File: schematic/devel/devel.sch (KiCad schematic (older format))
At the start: 108 parts

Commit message: converted schematic to flat hierarchical
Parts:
- removed C? (x2): 330n, symbol Device:C_Small
- removed C? (x2): 10u, symbol Device:CP_Small
- removed C? (x3): 1u, symbol Device:CP_Small
- removed C?: 22u, symbol Device:C_Small
- removed C?: 2.2u, symbol Device:CP_Small
- removed C? (x11): 100n, symbol Device:C_Small
- removed C?: 10n, symbol Device:C_Small
- removed C? (x4): 4p, symbol Device:C_Small
- removed D? (x4): 1N4001, Diode_THT:D_DO-41_SOD81_P10.16mm_Horizontal, symbol Diode:1N4001
- removed D?: S599x, symbol common:S599x
- removed D? (x2): 1N4148, Diode_THT:D_DO-35_SOD27_P7.62mm_Horizontal, symbol Diode:1N4148
- removed J?: CONN_PWR, symbol Connector:Conn_01x03_Male
- removed J?: X1, symbol Connector:Conn_Coaxial
- removed J?: X2, symbol Connector:Conn_Coaxial
- removed J?: Y1, symbol Connector:Conn_Coaxial
- removed J?: Y2, symbol Connector:Conn_Coaxial
- removed J?: DIFFX, symbol Connector:Conn_Coaxial
- removed J?: DIFFY, symbol Connector:Conn_Coaxial
- removed J?: SUM, symbol Connector:Conn_Coaxial
- removed J?: POSX, symbol Connector:Conn_Coaxial
- removed J?: POSY, symbol Connector:Conn_Coaxial
- removed R?: 100, symbol Device:R_Small
- removed R? (x4): 100k, symbol Device:R_Small
- removed R? (x18): 1k, symbol Device:R_Small
- removed R? (x9): 50, symbol Device:R_Small
- removed TP? (x6): TestPoint, symbol Connector:TestPoint
- removed U?: REF5010IDGK, Package_SO:MSOP-8_3x3mm_P0.65mm, symbol Reference_Voltage:REF5010IDGK
- removed U?: L7812, symbol Regulator_Linear:L7812
- removed U?: L7912, symbol Regulator_Linear:L7912
- removed U? (x23): OPA4197, symbol Device:Opamp_Quad_Generic
- removed U? (x2): AD538, symbol common:AD538
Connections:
- net labels removed: +10V, +12V, +15V, -12V, -15V, -X1, -X2, -Y1, -Y2, DIFFX, DIFFY, GND, POSX, POSY, SUM
- wire segments 398 -> 0
- no-connect marks 20 -> 0
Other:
- note removed: "BIAS VOLTAGE"
- note removed: "BUFFERED OUTPUT CONNECTORS"
- note removed: "DIVISION ARTHIMETIC"
- note removed: "LINEAR ARTHIMETIC"
- note removed: "POSITION-SENSITIVE DETECTOR AND TRANSIMPEDANCE AMPLIFIER"
- note removed: "POWER CONNECTOR"
- note removed: "SUPPLY VOLTAGE"

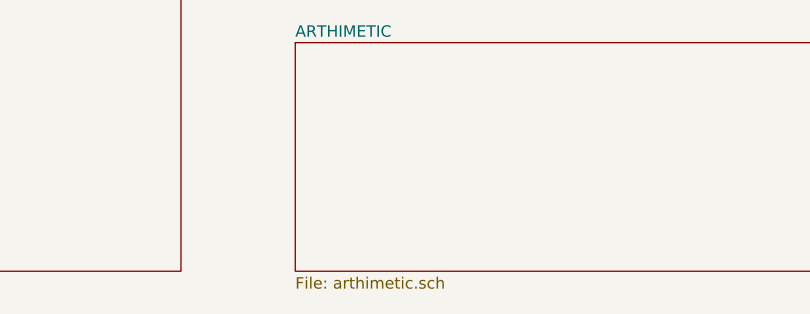
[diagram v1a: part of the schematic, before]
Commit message: fixed arithmetic typo, decoupling cap polarisation
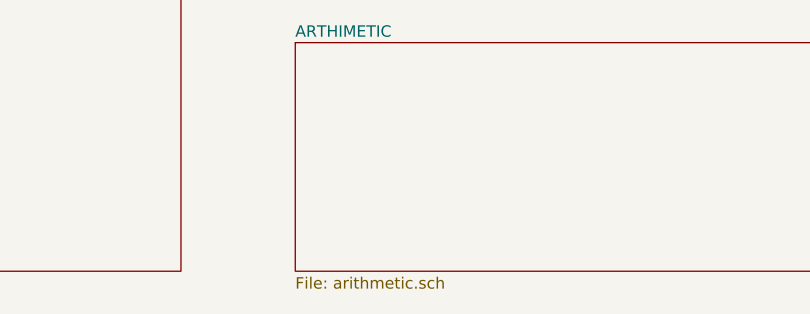
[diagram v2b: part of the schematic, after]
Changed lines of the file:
@@
 U 5D894F76
 F0 "ARTHIMETIC" 50
-F1 "arthimetic.sch" 50
+F1 "arithmetic.sch" 50
 $EndSheet
 $Sheet

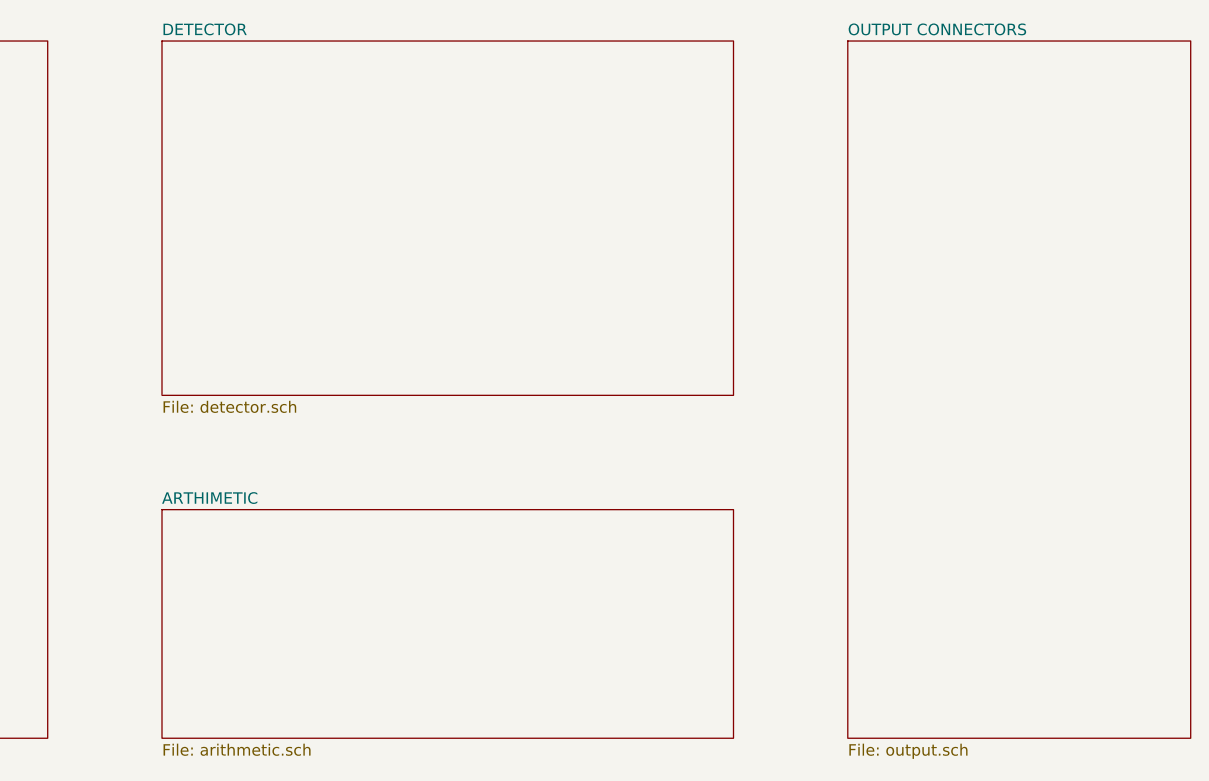
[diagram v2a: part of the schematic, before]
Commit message: removed arithmetic unit from development board, changed output connectors
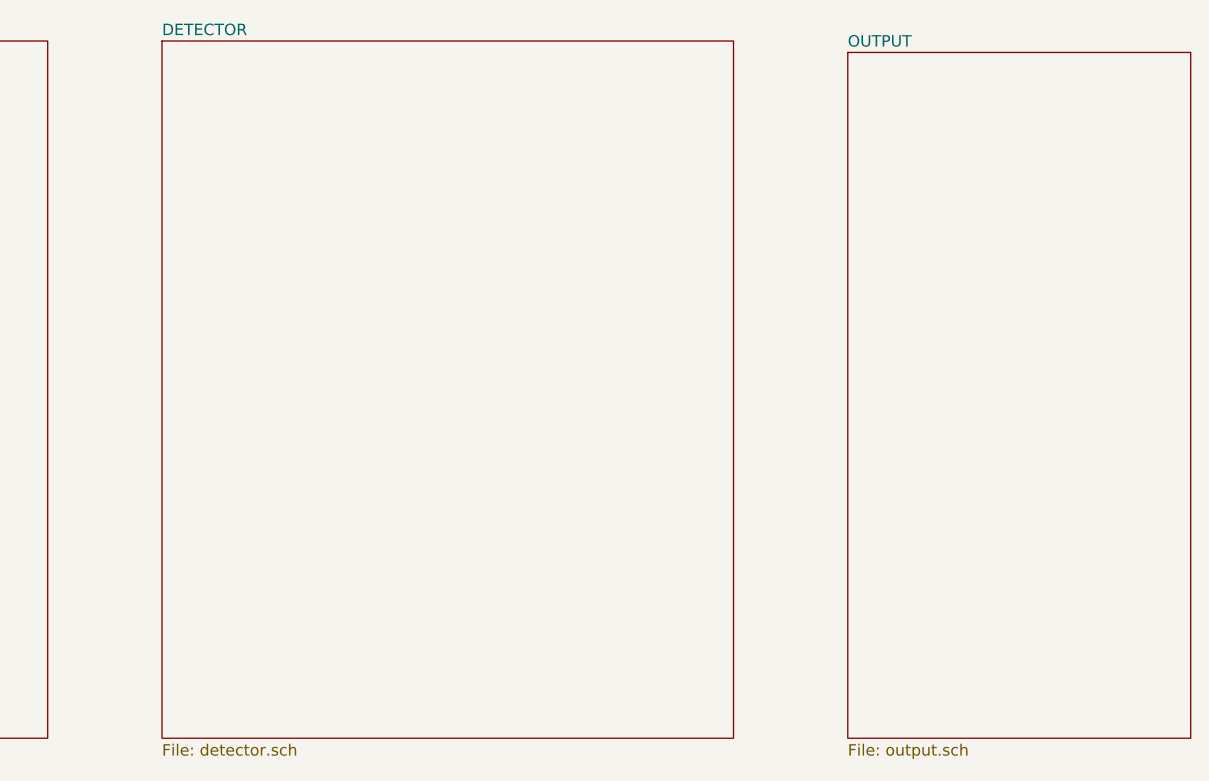
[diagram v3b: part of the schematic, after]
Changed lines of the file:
@@
 $Descr A4 11693 8268
 encoding utf-8
-Sheet 1 5
+Sheet 1 4
 Title "Position-sensitive Detector Development Board"
 Date "2019-03-21"
@@
 $EndSheet
 $Sheet
-S 4500 4500 2500 1000
-U 5D894F76
-F0 "ARTHIMETIC" 50
-F1 "arithmetic.sch" 50
-$EndSheet
-$Sheet
-S 7500 2450 1500 3050
-U 5D911A34
-F0 "OUTPUT CONNECTORS" 50
-F1 "output.sch" 50
-$EndSheet
-$Sheet
-S 4500 2450 2500 1550
+S 4500 2450 2500 3050
 U 5D929D0E
 F0 "DETECTOR" 50
 F1 "detector.sch" 50
 $EndSheet
+$Sheet
+S 7500 2500 1500 3000
+U 5C9BDA7E
+F0 "OUTPUT" 50
+F1 "output.sch" 50
+$EndSheet
 $EndSCHEMATC

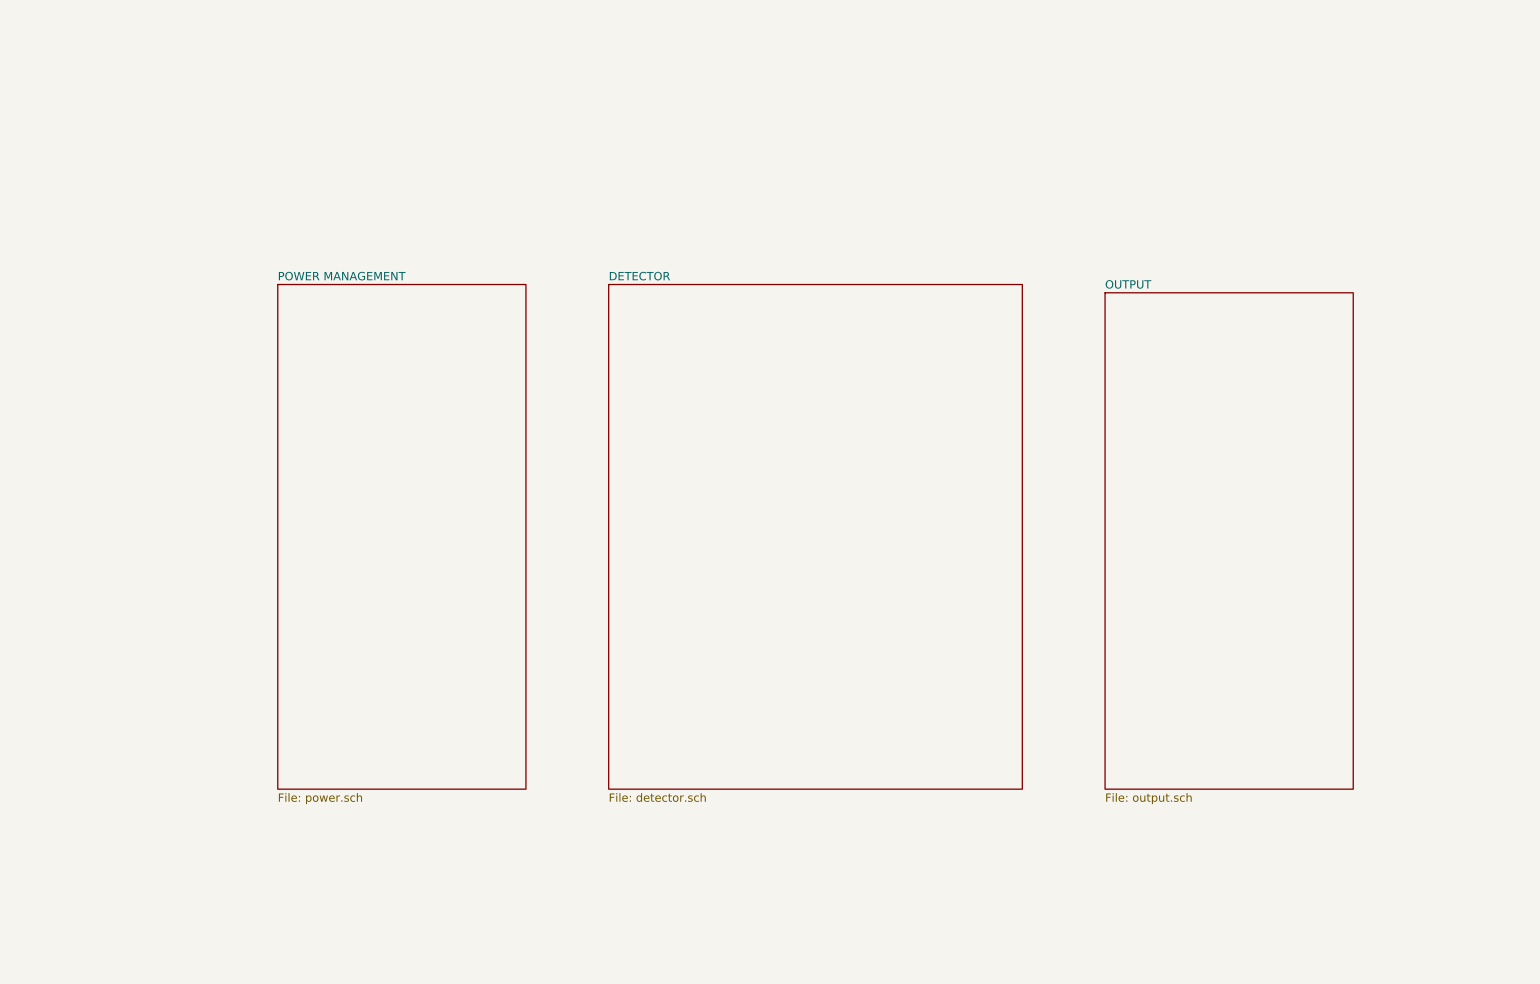
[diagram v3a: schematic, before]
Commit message: merged circuit sheets to single sheet, removed extra diodes, changed diode type
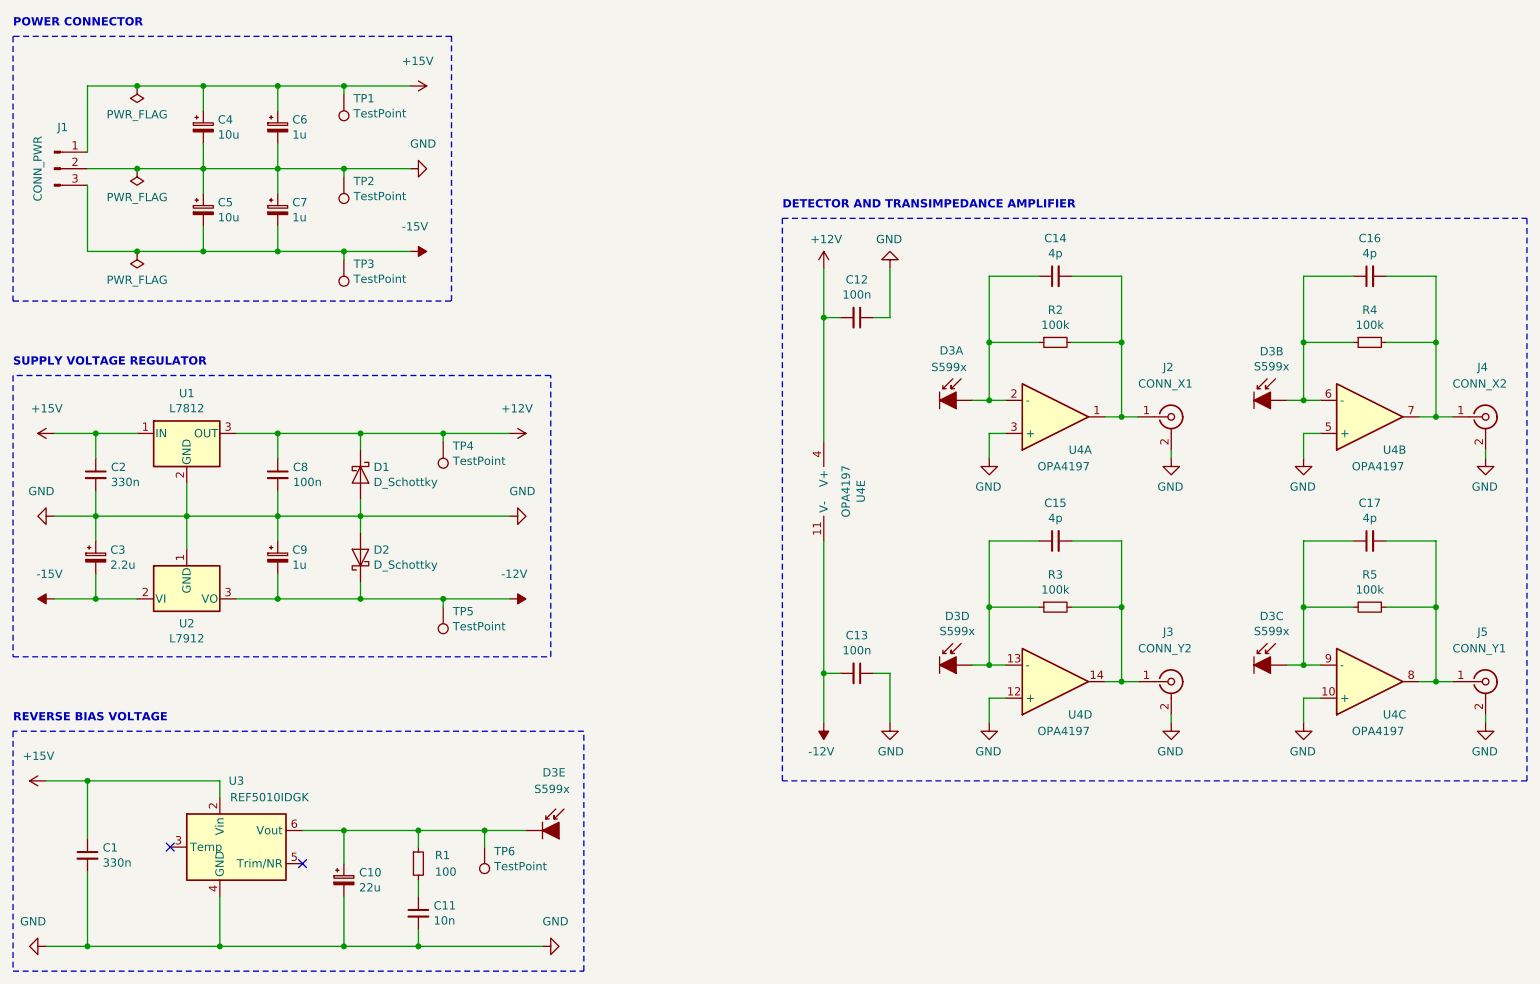
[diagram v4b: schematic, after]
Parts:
- added C1: 330n, Capacitor_SMD:C_0603_1608Metric, symbol Device:C_Small
- added C10: 22u, Capacitor_SMD:CP_Elec_5x5.4, symbol Device:CP_Small
- added C11: 10n, Capacitor_SMD:C_0402_1005Metric, symbol Device:C_Small
- added C12, C13, C8: 100n, Capacitor_SMD:C_0603_1608Metric, symbol Device:C_Small
- added C14, C15, C16, C17: 4p, Capacitor_SMD:C_0402_1005Metric, symbol Device:C_Small
- added C2: 330n, Capacitor_SMD:C_0805_2012Metric, symbol Device:C_Small
- added C3: 2.2u, Capacitor_SMD:CP_Elec_4x5.4, symbol Device:CP_Small
- added C4, C5: 10u, Capacitor_SMD:CP_Elec_4x5.4, symbol Device:CP_Small
- added C6, C7: 1u, Capacitor_SMD:CP_Elec_4x5.4, symbol Device:CP_Small
- added C9: 1u, Capacitor_SMD:CP_Elec_5x4.4, symbol Device:CP_Small
- added D1, D2: D_Schottky, Diode_SMD:D_SMA, symbol Device:D_Schottky
- added D3: S599x, Sensor_OpticalPosition:S5990, symbol Sensor_OpticalPosition:S599x
- added J1: CONN_PWR, Connector_PinHeader_1.00mm:PinHeader_1x03_P1.00mm_Vertical, symbol Connector:Conn_01x03_Male
- added J2: CONN_X1, Connector_Coaxial:SMA_Amphenol_901-144_Vertical, symbol Connector:Conn_Coaxial
- added J3: CONN_Y2, Connector_Coaxial:SMA_Amphenol_901-144_Vertical, symbol Connector:Conn_Coaxial
- added J4: CONN_X2, Connector_Coaxial:SMA_Amphenol_901-144_Vertical, symbol Connector:Conn_Coaxial
- added J5: CONN_Y1, Connector_Coaxial:SMA_Amphenol_901-144_Vertical, symbol Connector:Conn_Coaxial
- added R1: 100, Resistor_SMD:R_0603_1608Metric, symbol Device:R_Small
- added R2, R3, R4, R5: 100k, Resistor_SMD:R_0805_2012Metric, symbol Device:R_Small
- added TP1, TP2, TP3, TP4, TP5, TP6: TestPoint, TestPoint:TestPoint_Bridge_Pitch2.54mm_Drill0.7mm, symbol Connector:TestPoint
- added U1: L7812, Package_TO_SOT_SMD:TO-252-2, symbol Regulator_Linear:L7812
- added U2: L7912, Package_TO_SOT_SMD:TO-252-2, symbol Regulator_Linear:L7912
- added U3: REF5010IDGK, Package_SO:MSOP-8_3x3mm_P0.65mm, symbol Reference_Voltage:REF5010IDGK
- added U4: OPA4197, Package_SO:TSSOP-14_4.4x5mm_P0.65mm, symbol Device:Opamp_Quad_Generic
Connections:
- new net: C14.1, D3.1 (I1), R2.1, U4.2 (-)
- new net: C16.1, D3.6 (I2), R4.1, U4.6 (-)
- new net: C16.2, J4.1 (In), R4.2, U4.7
- new net: C17.1, D3.10 (I4), R5.1, U4.9 (-)
- new net: C17.2, J5.1 (In), R5.2, U4.8
- new net: C14.2, J2.1 (In), R2.2, U4.1
- new net: C15.1, D3.5 (I3), R3.1, U4.13 (-)
- new net: C15.2, J3.1 (In), R3.2, U4.14
- new net: C10.1, D3.8 (K), R1.1, TP6.1, U3.6 (Vout)
- new net: C11.1, R1.2
- new net +12V: C12.2, C8.1, D1.1 (K), TP4.1, U1.3 (OUT), U4.4 (V+)
- new net +15V: C1.1, C2.1, C4.1, C6.1, J1.1 (Pin_1), TP1.1, U1.1 (IN), U3.2 (Vin)
- new net -12V: C13.2, C9.2, D2.1 (K), TP5.1, U2.3 (VO), U4.11 (V-)
- new net -15V: C3.2, C5.2, C7.2, J1.3 (Pin_3), TP3.1, U2.2 (VI)
- new net GND: C1.2, C10.2, C11.2, C12.1, C13.1, C2.2, C3.1, C4.2, C5.1, C6.2, C7.1, C8.2, C9.1, D1.2 (A), D2.2 (A), J1.2 (Pin_2), J2.2 (Ext), J3.2 (Ext), J4.2 (Ext), J5.2 (Ext), TP2.1, U1.2 (GND), U2.1 (GND), U3.4 (GND), U4.10 (+), U4.12 (+), U4.3 (+), U4.5 (+)
- no-connect marks 0 -> 2
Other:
- note added: "DETECTOR AND TRANSIMPEDANCE AMPLIFIER"
- note added: "POWER CONNECTOR"
- note added: "REVERSE BIAS VOLTAGE"
- note added: "SUPPLY VOLTAGE REGULATOR"

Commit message: reassigned footprints that were not smd compatible
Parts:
- J1: footprint Connector_PinHeader_1.00mm:PinHeader_1x03_P1.00mm_Vertical -> Connector_PinHeader_2.00mm:PinHeader_1x03_P2.00mm_Vertical_SMD_Pin1Left
- J2, J3, J4, J5: footprint Connector_Coaxial:SMA_Amphenol_901-144_Vertical -> Connector_Coaxial:SMA_Amphenol_132289_EdgeMount
- TP1, TP2, TP3, TP4, TP5, TP6: footprint TestPoint:TestPoint_Bridge_Pitch2.54mm_Drill0.7mm -> TestPoint:TestPoint_Pad_D1.0mm
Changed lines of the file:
@@
 F 0 "J3" H 7850 5150 50  0000 L CNN
 F 1 "CONN_Y2" H 7700 5050 50  0000 L CNN
-F 2 "Connector_Coaxial:SMA_Amphenol_901-144_Vertical" H 7900 4850 50  0001 C CNN
+F 2 "Connector_Coaxial:SMA_Amphenol_132289_EdgeMount" H 7900 4850 50  0001 C CNN
 F 3 " ~" H 7900 4850 50  0001 C CNN
 	1    7900 4850
@@
 F 0 "J5" H 9750 5150 50  0000 L CNN
 F 1 "CONN_Y1" H 9600 5050 50  0000 L CNN
-F 2 "Connector_Coaxial:SMA_Amphenol_901-144_Vertical" H 9800 4850 50  0001 C CNN
+F 2 "Connector_Coaxial:SMA_Amphenol_132289_EdgeMount" H 9800 4850 50  0001 C CNN
 F 3 " ~" H 9800 4850 50  0001 C CNN
 	1    9800 4850
@@
 F 0 "J4" H 9750 3550 50  0000 L CNN
 F 1 "CONN_X2" H 9600 3450 50  0000 L CNN
-F 2 "Connector_Coaxial:SMA_Amphenol_901-144_Vertical" H 9800 3250 50  0001 C CNN
+F 2 "Connector_Coaxial:SMA_Amphenol_132289_EdgeMount" H 9800 3250 50  0001 C CNN
 F 3 " ~" H 9800 3250 50  0001 C CNN
 	1    9800 3250
@@
 F 0 "J2" H 7850 3550 50  0000 L CNN
 F 1 "CONN_X1" H 7700 3450 50  0000 L CNN
-F 2 "Connector_Coaxial:SMA_Amphenol_901-144_Vertical" H 7900 3250 50  0001 C CNN
+F 2 "Connector_Coaxial:SMA_Amphenol_132289_EdgeMount" H 7900 3250 50  0001 C CNN
 F 3 " ~" H 7900 3250 50  0001 C CNN
 	1    7900 3250
@@
 F 0 "TP1" H 2842 1326 50  0000 R CNN
 F 1 "TestPoint" H 2842 1417 50  0000 R CNN
-F 2 "TestPoint:TestPoint_Bridge_Pitch2.54mm_Drill0.7mm" H 3100 1300 50  0001 C CNN
+F 2 "TestPoint:TestPoint_Pad_D1.0mm" H 3100 1300 50  0001 C CNN
 F 3 "~" H 3100 1300 50  0001 C CNN
 	1    2900 1300
@@
 F 0 "TP2" H 2842 1826 50  0000 R CNN
 F 1 "TestPoint" H 2842 1917 50  0000 R CNN
-F 2 "TestPoint:TestPoint_Bridge_Pitch2.54mm_Drill0.7mm" H 3100 1800 50  0001 C CNN
+F 2 "TestPoint:TestPoint_Pad_D1.0mm" H 3100 1800 50  0001 C CNN
 F 3 "~" H 3100 1800 50  0001 C CNN
 	1    2900 1800
@@
 F 0 "TP3" H 2842 2326 50  0000 R CNN
 F 1 "TestPoint" H 2842 2417 50  0000 R CNN
-F 2 "TestPoint:TestPoint_Bridge_Pitch2.54mm_Drill0.7mm" H 3100 2300 50  0001 C CNN
+F 2 "TestPoint:TestPoint_Pad_D1.0mm" H 3100 2300 50  0001 C CNN
 F 3 "~" H 3100 2300 50  0001 C CNN
 	1    2900 2300
@@
 F 0 "J1" H 1200 2000 50  0000 C CNN
 F 1 "CONN_PWR" V 1050 1750 50  0000 C CNN
-F 2 "Connector_PinHeader_1.00mm:PinHeader_1x03_P1.00mm_Vertical" H 1150 1750 50  0001 C CNN
+F 2 "Connector_PinHeader_2.00mm:PinHeader_1x03_P2.00mm_Vertical_SMD_Pin1Left" H 1150 1750 50  0001 C CNN
 F 3 "~" H 1150 1750 50  0001 C CNN
 	1    1150 1750
@@
 F 0 "TP5" H 3442 4426 50  0000 R CNN
 F 1 "TestPoint" H 3442 4517 50  0000 R CNN
-F 2 "TestPoint:TestPoint_Bridge_Pitch2.54mm_Drill0.7mm" H 3700 4400 50  0001 C CNN
+F 2 "TestPoint:TestPoint_Pad_D1.0mm" H 3700 4400 50  0001 C CNN
 F 3 "~" H 3700 4400 50  0001 C CNN
 	1    3500 4400
@@
 F 0 "TP4" H 3442 3426 50  0000 R CNN
 F 1 "TestPoint" H 3442 3517 50  0000 R CNN
-F 2 "TestPoint:TestPoint_Bridge_Pitch2.54mm_Drill0.7mm" H 3700 3400 50  0001 C CNN
+F 2 "TestPoint:TestPoint_Pad_D1.0mm" H 3700 3400 50  0001 C CNN
 F 3 "~" H 3700 3400 50  0001 C CNN
 	1    3500 3400
@@
 F 0 "TP6" H 3692 5876 50  0000 R CNN
 F 1 "TestPoint" H 3692 5967 50  0000 R CNN
-F 2 "TestPoint:TestPoint_Bridge_Pitch2.54mm_Drill0.7mm" H 3950 5850 50  0001 C CNN
+F 2 "TestPoint:TestPoint_Pad_D1.0mm" H 3950 5850 50  0001 C CNN
 F 3 "~" H 3950 5850 50  0001 C CNN
 	1    3750 5850

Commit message: created first pcb layout draft
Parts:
- C12, C13: footprint Capacitor_SMD:C_0603_1608Metric -> Capacitor_SMD:C_0201_0603Metric
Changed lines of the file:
@@
 F 0 "C12" V 5771 2650 50  0000 C CNN
 F 1 "100n" V 5862 2650 50  0000 C CNN
-F 2 "Capacitor_SMD:C_0603_1608Metric" H 6000 2650 50  0001 C CNN
+F 2 "Capacitor_SMD:C_0201_0603Metric" H 6000 2650 50  0001 C CNN
 F 3 "~" H 6000 2650 50  0001 C CNN
 	1    6000 2650
@@
 F 0 "C13" V 5771 4800 50  0000 C CNN
 F 1 "100n" V 5862 4800 50  0000 C CNN
-F 2 "Capacitor_SMD:C_0603_1608Metric" H 6000 4800 50  0001 C CNN
+F 2 "Capacitor_SMD:C_0201_0603Metric" H 6000 4800 50  0001 C CNN
 F 3 "~" H 6000 4800 50  0001 C CNN
 	1    6000 4800
